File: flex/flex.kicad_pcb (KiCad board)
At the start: 2 copper layers, 74.1 x 41.5 mm, 29 parts, among them J1 Conn_01x06_Female, J2 Conn_01x03_Female, J3 Conn_01x01_Female, SW1 SW_Push, SW14 SW_Push, SW19 SW_Push, SW5 SW_Push, SW9 SW_Push

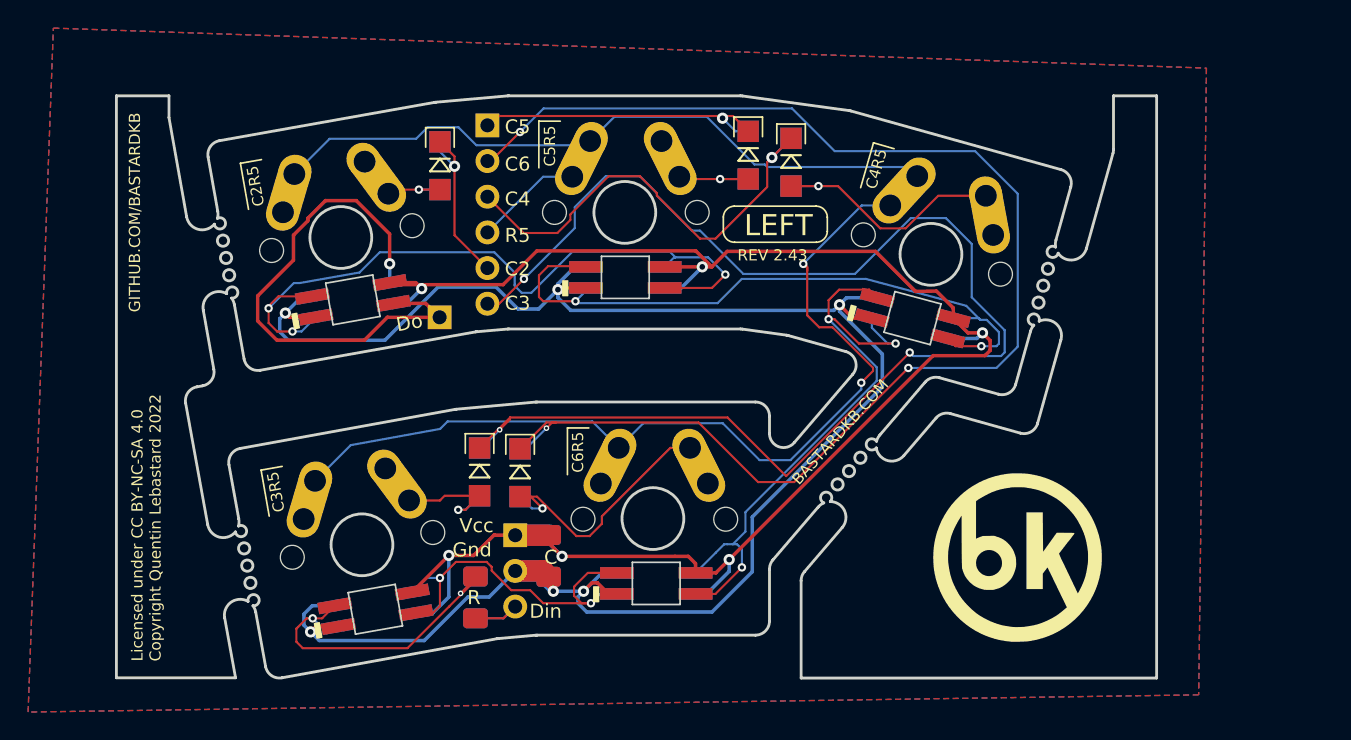
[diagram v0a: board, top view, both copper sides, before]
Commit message: move rgb connector
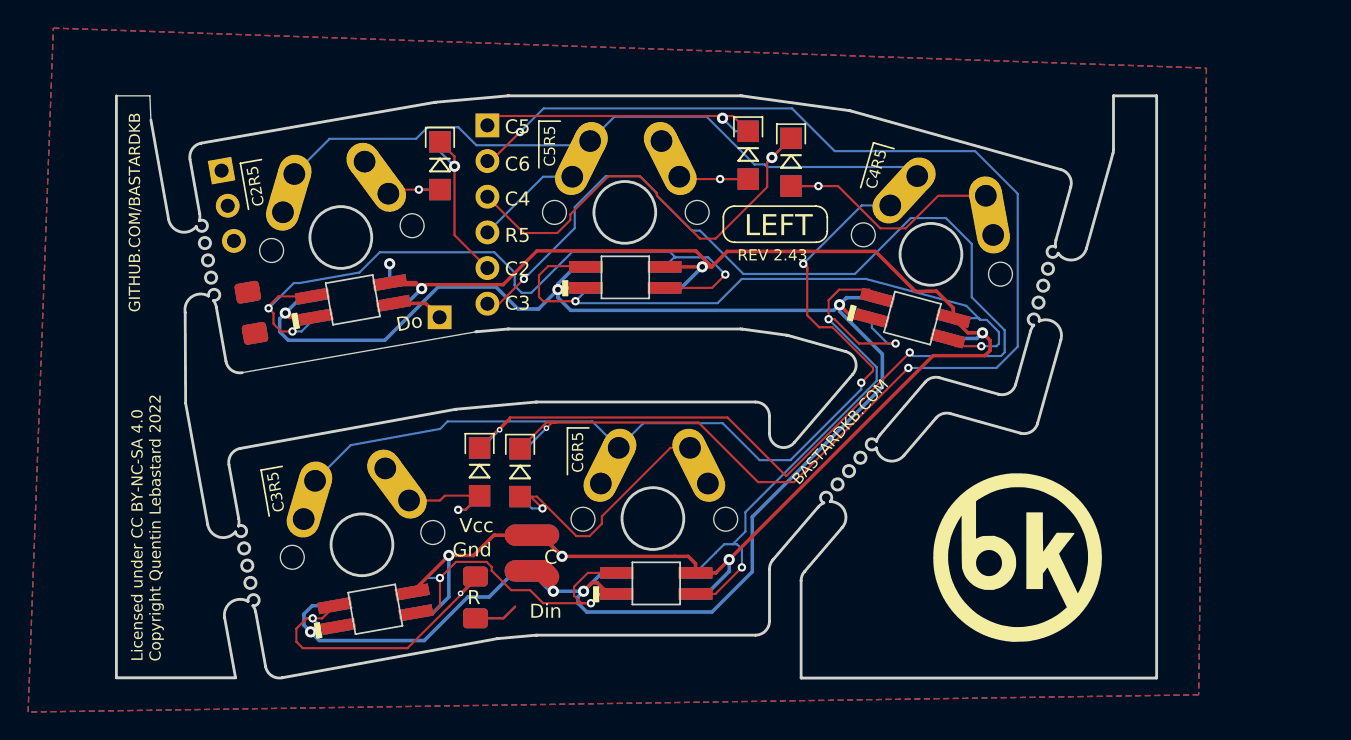
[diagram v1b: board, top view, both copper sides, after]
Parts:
- moved J2 33.3 mm to (65.5, 71.6), turned to 10 degrees
- moved C1 27.3 mm to (67.6, 81.7), turned to -80 degrees
- moved C2 27.3 mm to (67.6, 81.7), turned to -80 degrees
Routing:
- net Net-(D12-Pad1): track 37.5 -> 5.04 mm
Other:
- outline, holes or cut-outs redrawn

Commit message: vcc gnd routing
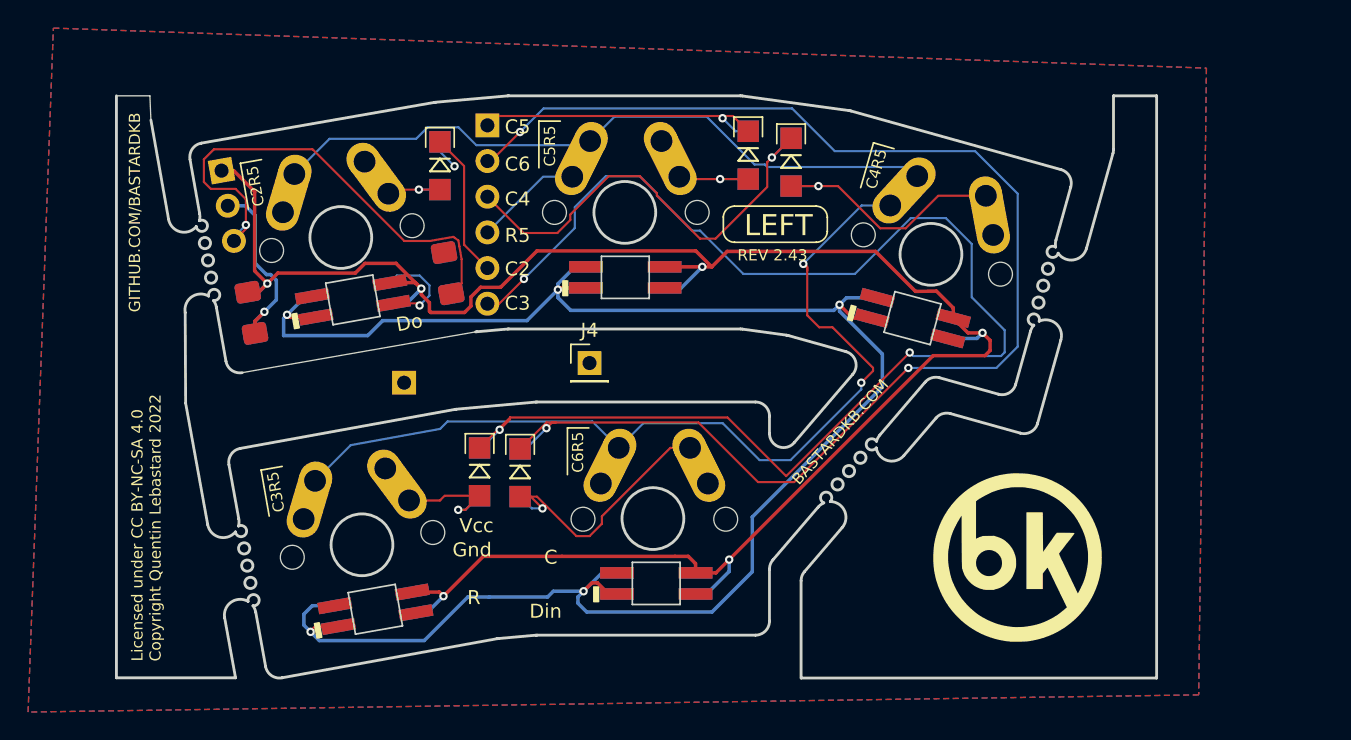
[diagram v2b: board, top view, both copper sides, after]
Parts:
- added J4: Conn_01x01_Female, Connector_PinHeader_2.54mm:PinHeader_1x01_P2.54mm_Vertical, F.Cu at (91.7, 85.3)
- moved R1 23.2 mm to (81.6, 78.9), turned to -80 degrees
- moved R2 23.2 mm to (81.6, 78.9), turned to -80 degrees
- moved J3 5.30 mm to (78.5, 86.7)
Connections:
- D10 pad 1: Net-(D10-Pad1) -> Net-(D11-Pad1)
- D10 pad 3: Net-(D10-Pad3) -> Net-(D12-Pad1)
- D11 pad 1: Net-(D10-Pad1) -> Net-(D11-Pad1)
- D11 pad 3: Net-(D10-Pad3) -> Net-(D12-Pad1)
- D12 pad 3: Net-(D10-Pad1) -> Net-(D12-Pad3)
- D13 pad 3: Net-(D10-Pad1) -> Net-(D12-Pad3)
- D2 pad 1: Net-(D2-Pad1) -> Net-(D3-Pad1)
- D2 pad 3: Net-(D2-Pad3) -> Net-(D4-Pad1)
- D3 pad 1: Net-(D2-Pad1) -> Net-(D3-Pad1)
- D3 pad 3: Net-(D2-Pad3) -> Net-(D4-Pad1)
- D4 pad 3: Net-(D2-Pad1) -> Net-(D7-Pad1)
- D6 pad 3: Net-(D2-Pad1) -> Net-(D7-Pad1)
- D7 pad 1: Net-(D10-Pad3) -> Net-(D7-Pad1)
- D7 pad 3: Net-(D4-Pad1) -> Net-(D11-Pad1)
- D8 pad 1: Net-(D10-Pad3) -> Net-(D7-Pad1)
- D8 pad 3: Net-(D4-Pad1) -> Net-(D11-Pad1)
- J3 pad 1: Net-(D12-Pad1) -> Net-(D3-Pad1)
- R1 pad 1: Net-(D2-Pad3) -> Net-(D12-Pad3)
- R2 pad 1: Net-(D2-Pad3) -> Net-(D12-Pad3)
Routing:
- net Net-(D10-Pad1): track 51.8 -> 0.00 mm, vias 3 -> 0
- net Net-(D10-Pad3): track 47.9 -> 0.00 mm, vias 2 -> 0
- net Net-(D4-Pad1): track 45.1 -> 0.00 mm, vias 3 -> 0
- net Din: track 6.35 -> 35.9 mm, vias 0 -> 1
- net Net-(D2-Pad1): track 26.5 -> 0.00 mm, vias 2 -> 0
- net Net-(D2-Pad3): track 24.9 -> 0.00 mm, vias 2 -> 0
- net Vcc: track 128.6 -> 144.6 mm
- net Gnd: track 139.2 -> 144.6 mm
- net Net-(D12-Pad1): track 5.04 -> 6.97 mm

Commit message: connect all signals per led
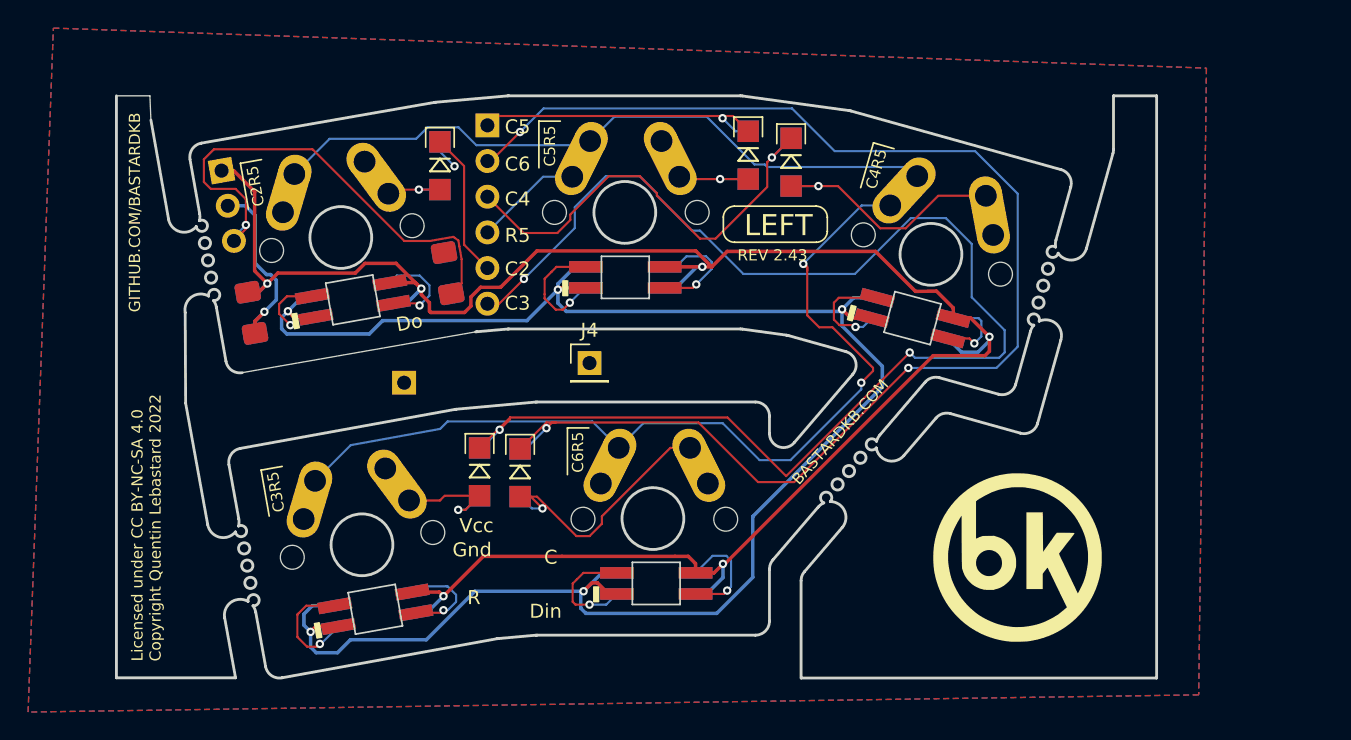
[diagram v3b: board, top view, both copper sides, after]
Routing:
- net Net-(D4-Pad1): track 0.00 -> 16.1 mm, vias 0 -> 2
- net Net-(D11-Pad1): track 0.00 -> 15.9 mm, vias 0 -> 2
- net Net-(D7-Pad1): track 0.00 -> 14.2 mm, vias 0 -> 2
- net Net-(D12-Pad1): track 6.97 -> 15.6 mm, vias 1 -> 2
- net Net-(D3-Pad1): track 0.00 -> 7.23 mm, vias 0 -> 1
- net Net-(D12-Pad3): track 0.00 -> 6.48 mm, vias 0 -> 1
- net Gnd: track 144.6 -> 145.7 mm
- net Vcc: track 144.6 -> 145.5 mm

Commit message: connect led signals
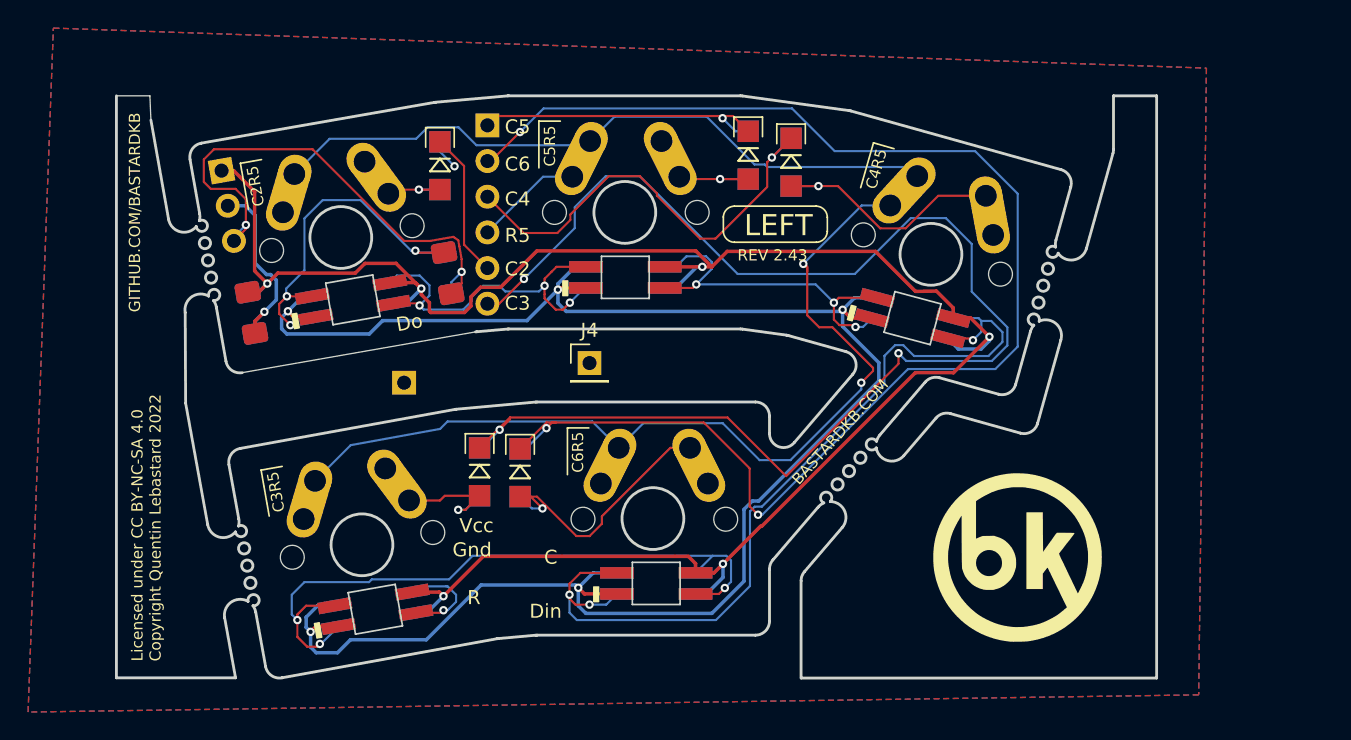
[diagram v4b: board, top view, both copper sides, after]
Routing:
- net Net-(D7-Pad1): track 14.2 -> 62.2 mm, vias 2 -> 3
- net Net-(D4-Pad1): track 16.1 -> 49.0 mm, vias 2 -> 3
- net Net-(D12-Pad3): track 6.48 -> 26.7 mm, vias 1 -> 3
- net Net-(D11-Pad1): track 15.9 -> 26.2 mm, vias 2 -> 3
- net Net-(D12-Pad1): track 15.6 -> 25.8 mm, vias 2 -> 3
- net col6: track 98.0 -> 101.5 mm
- net Din: track 35.9 -> 37.8 mm, vias 1 -> 2
- net Vcc: track 145.5 -> 144.7 mm

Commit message: drc
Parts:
- J3, J4: footprint Connector_PinHeader_2.54mm:PinHeader_1x01_P2.54mm_Vertical -> custom:PinHeader_1x01_P2.54mm_Vertical
- moved J4 17.3 mm to (105.9, 75.4)
- moved J3 12.8 mm to (85.3, 97.5)
- moved D5 0.25 mm to (80.8, 66.2)
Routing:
- net Net-(D7-Pad1): track 62.2 -> 85.9 mm, vias 3 -> 5
- net Net-(D3-Pad1): track 7.23 -> 13.4 mm, vias 1 -> 2
- net col6: track 101.5 -> 100.3 mm
- net Din: track 37.8 -> 37.1 mm
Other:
- board text added: "3 ROWS"
- board text removed: "Din"
- board text removed: "Gnd"

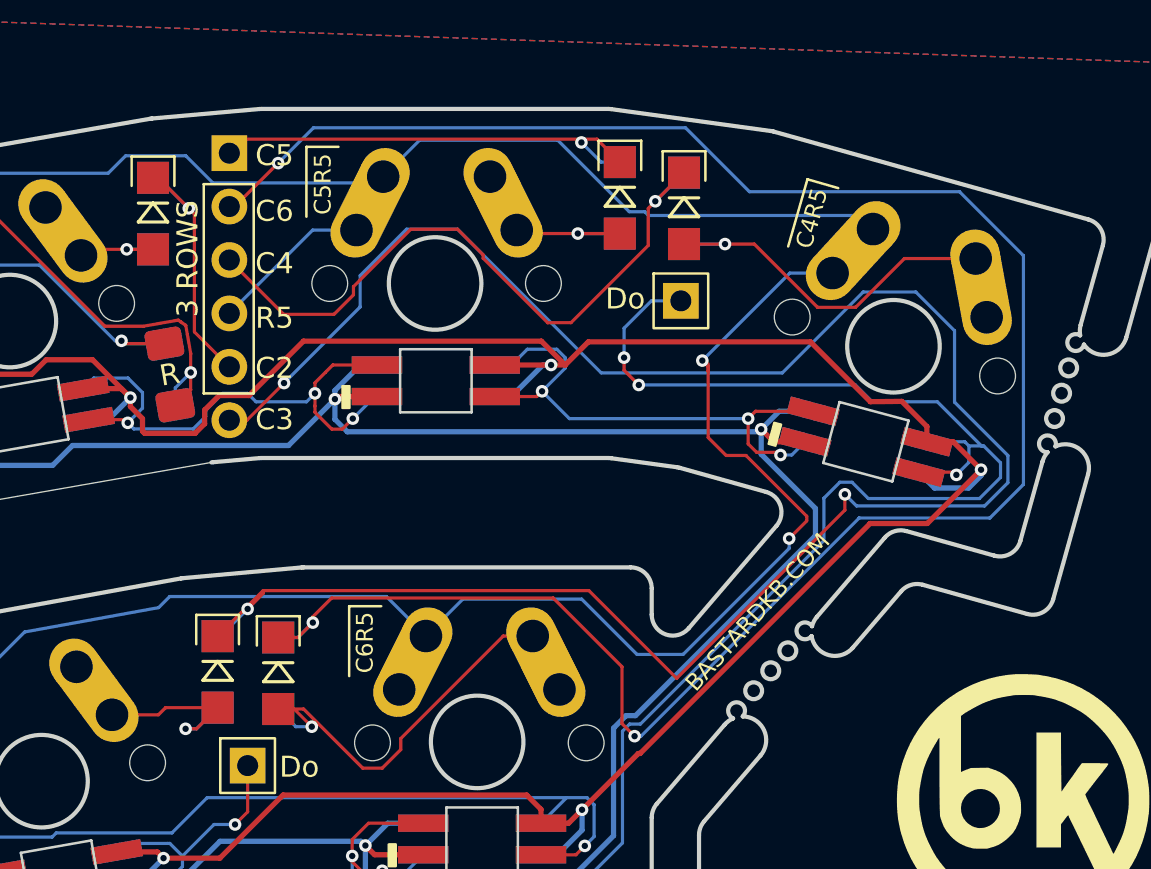
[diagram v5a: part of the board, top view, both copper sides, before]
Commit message: flip c6 and c5
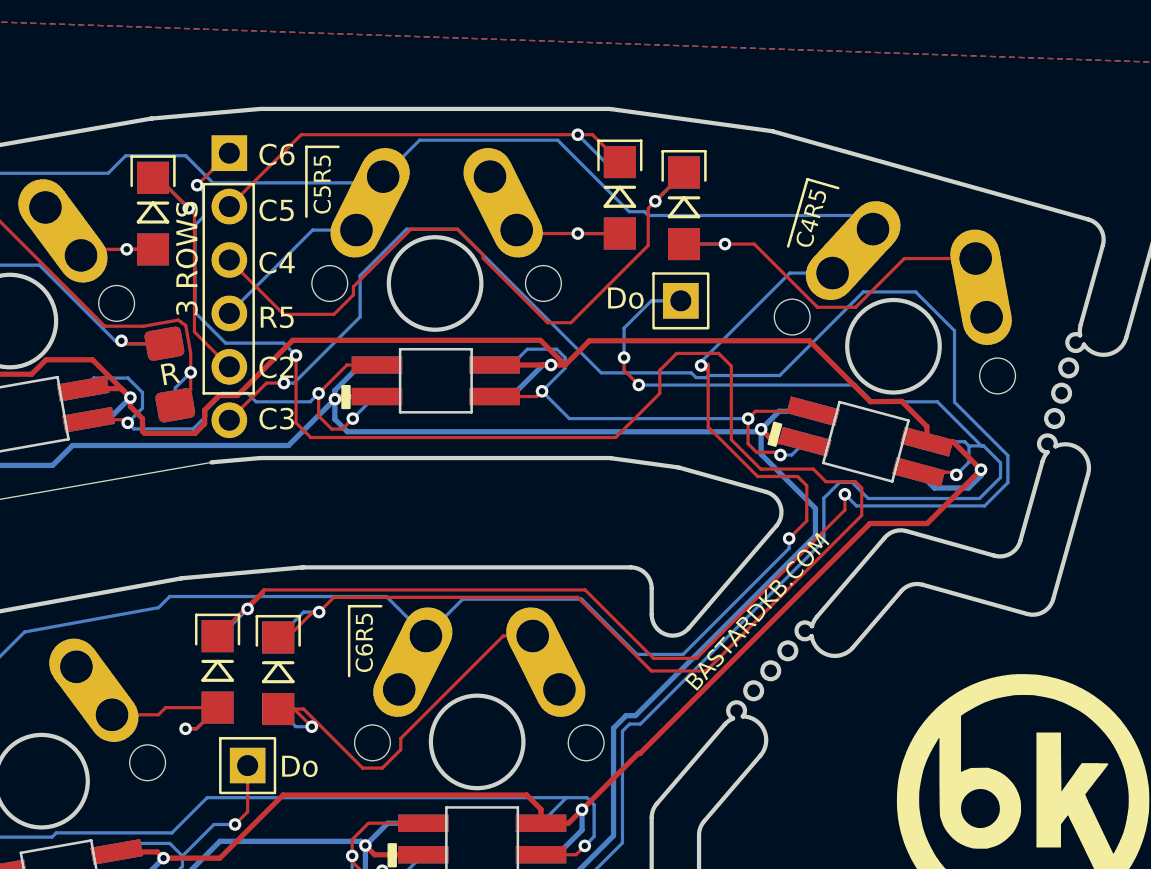
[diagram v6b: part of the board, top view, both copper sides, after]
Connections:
- J1 pad 1: col5 -> col6
- J1 pad 2: col6 -> col5
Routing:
- net col6: track 100.3 -> 88.3 mm
- net col5: track 21.5 -> 23.1 mm
- net row1: track 121.7 -> 122.3 mm

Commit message: silkscreen
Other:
- board text added: "REV 3.0"
- board text removed: "REV 2.43"
